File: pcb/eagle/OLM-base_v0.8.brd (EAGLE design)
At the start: 94.7 x 56.5 mm, 33 parts, among them IC1 ATMEGA, IC2 MCP1702-33, IC3 ENC28J60SP, J1 MAGJACK, J2 POWER_JACKPTH, X1 16 MHz, X3 25MHz

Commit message: changed logo
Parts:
- moved FTDI 12.8 mm to (11.6, 54.2), turned to 0 degrees
- moved R6 7.39 mm to (28.7, 19.5)
- moved R9 6.78 mm to (28.8, 30.3)
- moved C7 3.83 mm to (28.6, 42.1)
- moved C8 3.76 mm to (21.1, 42.1)
- moved CX2 3.50 mm to (29.0, 9.42)
- moved C5 3.48 mm to (21.3, 3.28), turned to 180 degrees
- moved R7 2.69 mm to (22.3, 34.2)
- moved R8 2.67 mm to (22.3, 38.1)
- moved CX1 1.98 mm to (21.7, 28.4)
- moved L1 1.86 mm to (34.0, 3.38)
- moved IC3 1.17 mm to (37.9, 27.2), turned to 270 degrees
- moved C2 0.98 mm to (66.4, 42.7)
- moved R4 0.74 mm to (20.4, 7.52)
- moved IC1 0.72 mm to (77.2, 28.3)
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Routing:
- net PB1/D9/PWM: track 167.5 -> 89.0 mm, vias 1 -> 2
- net N$52: track 36.6 -> 75.3 mm, vias 0 -> 1
- net N$37: track 11.1 -> 45.3 mm
- net TD-: track 19.6 -> 52.7 mm, vias 0 -> 2
- net N$39: track 21.3 -> 52.2 mm, vias 0 -> 2
- net N$50: track 31.2 -> 60.1 mm, vias 0 -> 2
- net D0/RX: track 96.4 -> 70.1 mm, vias 1 -> 4
- net SCK/D13: track 167.0 -> 186.7 mm, vias 1 -> 3
- net D1/TX: track 108.5 -> 90.2 mm, vias 2 -> 4
- net N$53: track 22.7 -> 38.8 mm, vias 0 -> 1
- net D4: track 37.5 -> 53.3 mm, vias 1 -> 2
- net N$20: track 62.6 -> 47.3 mm, vias 3 -> 1
- net N$51: track 52.4 -> 37.5 mm, vias 1 -> 0
- net VCC: track 218.9 -> 233.7 mm
- net LEDB: track 58.0 -> 43.7 mm
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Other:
- board text added: "(cable)"
- board text added: "3.3V"
- board text added: "5V"
- board text added: "A"
- board text added: "D"
- board text added: "D/PWM"
- board text added: "DTR"
- board text added: "GND"
- board text added: "MISO"
- board text added: "MISO/D12"
- board text added: "MOSI"
- board text added: "MOSI/D11"
- board text added: "PB0"
- board text added: "PB1"
- board text added: "RST"
- board text added: "RX"
- board text added: "SCK"
- board text added: "SCK/D13"
- board text added: "SCL/A5"
- board text added: "SDA/A4"
- board text added: "TX"
- board text added: "http://pvos.org"
- board text added: "lab"
- board text added: "monitor"
- board text added: "olm connector"
- board text added: "open"
- board text added: "v_0.8"
- board text removed: "PVOS.org"
- board text removed: "olm_v0.8"

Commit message: changed logo
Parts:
- moved C7 3.48 mm to (25.5, 43.6), turned to 270 degrees
- moved C8 2.98 mm to (18.5, 43.6), turned to 270 degrees
- moved R6 1.61 mm to (28.8, 21.1)
- moved IC2 1.20 mm to (4.57, 23.0), turned to 0 degrees
- moved CON1 1.19 mm to (64.0, 50.6)
- moved R9 1.10 mm to (28.9, 31.4)
- moved CON4 1.09 mm to (64.3, 5.13)
- moved X3 0.86 mm to (20.5, 16.8)
- moved CON3 0.74 mm to (89.6, 17.4)
- moved CON2 0.60 mm to (89.6, 39.0)
- moved C4 0.40 mm to (21.7, 22.7)
- moved CX2 0.39 mm to (28.9, 9.80)
- moved C3 0.38 mm to (14.1, 23.6)
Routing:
- net N$37: track 45.3 -> 71.0 mm, vias 0 -> 1
- net N$1: track 31.9 -> 54.5 mm, vias 2 -> 1
- net N$52: track 75.3 -> 55.6 mm
- net MISO/D12: track 180.5 -> 164.1 mm
- net SCL/A5: track 101.3 -> 116.9 mm
- net PB0/D8: track 92.6 -> 78.5 mm, vias 3 -> 2
- net TCT: track 66.2 -> 52.2 mm
- net SCK/D13: track 186.7 -> 173.4 mm, vias 3 -> 2
- net D5/PWM: track 33.3 -> 23.2 mm
- net GND: track 329.5 -> 319.9 mm
- net PB1/D9/PWM: track 89.0 -> 98.2 mm
- net D4: track 53.3 -> 44.3 mm, vias 2 -> 1
- net D1/TX: track 90.2 -> 82.0 mm, vias 4 -> 0
- net D10/PWM: track 19.6 -> 27.0 mm
- net D0/RX: track 70.1 -> 63.1 mm, vias 4 -> 3
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
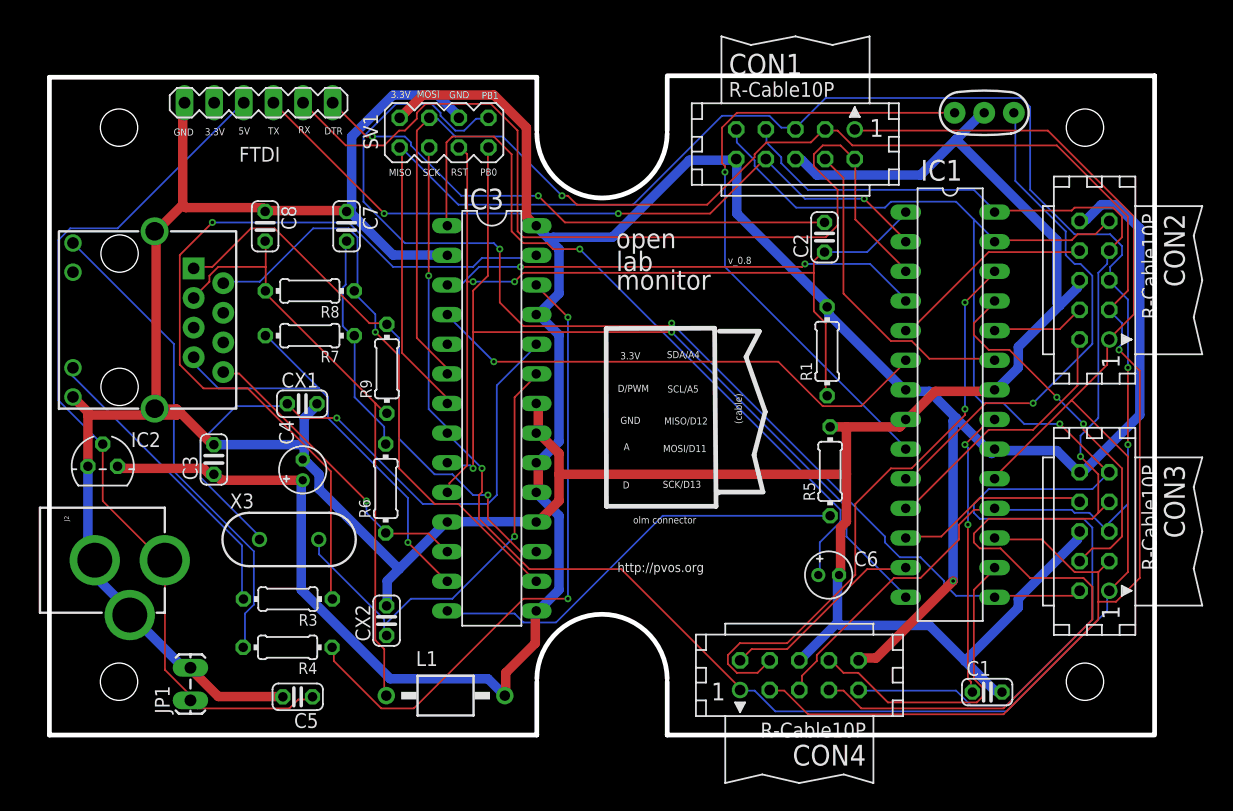
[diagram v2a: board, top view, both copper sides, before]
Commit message: fixed logo
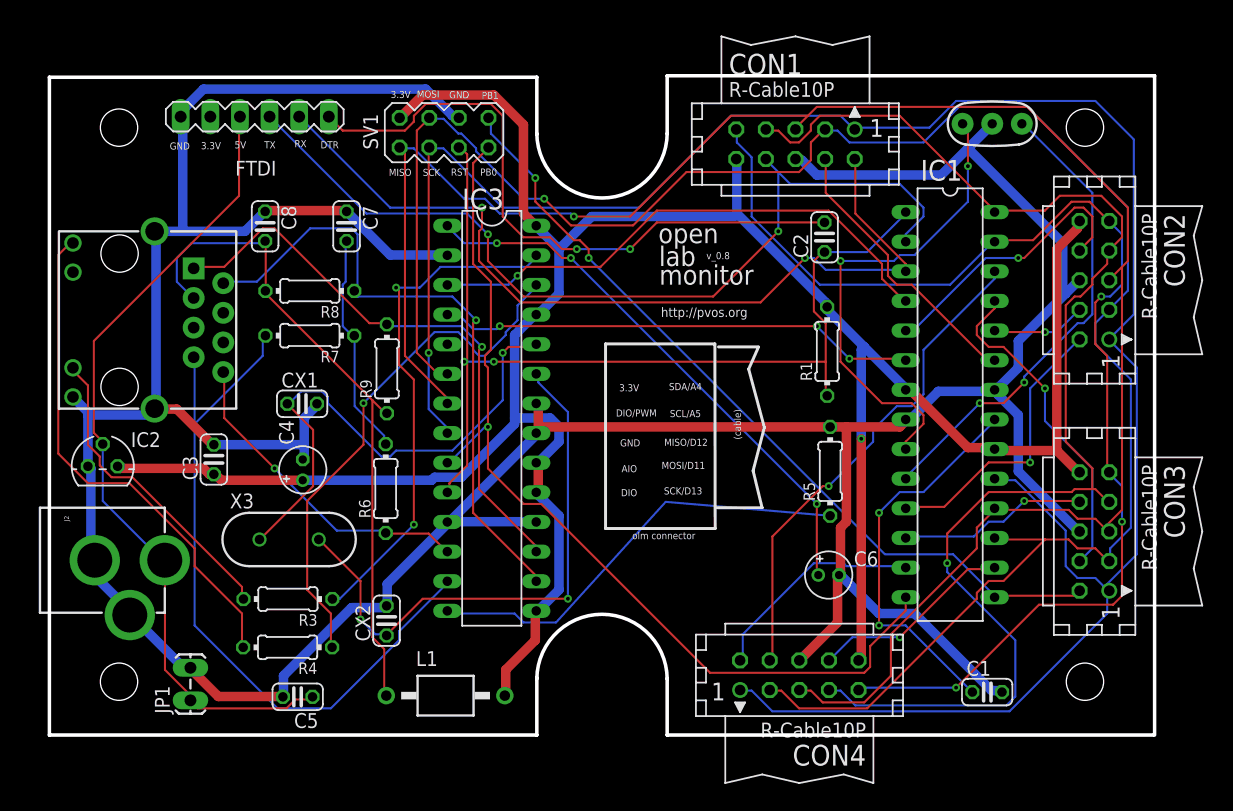
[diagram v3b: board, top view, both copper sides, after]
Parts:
- moved FTDI 1.24 mm to (11.3, 53.0)
- moved X1 1.16 mm to (80.8, 52.4)
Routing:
- net PB1/D9/PWM: track 98.2 -> 70.4 mm
- net N$37: track 71.0 -> 43.8 mm, vias 1 -> 2
- net RD+: track 39.8 -> 62.7 mm, vias 1 -> 0
- net SDA/A4: track 123.2 -> 105.8 mm, vias 1 -> 3
- net N$50: track 64.8 -> 47.8 mm, vias 1 -> 3
- net VCC: track 233.3 -> 216.7 mm
- net SCK/D13: track 173.4 -> 189.1 mm, vias 2 -> 1
- net D0/RX: track 63.1 -> 77.5 mm, vias 3 -> 2
- net N$1: track 54.5 -> 41.1 mm, vias 1 -> 2
- net N$52: track 55.6 -> 45.3 mm
- net D10/PWM: track 27.0 -> 17.6 mm, vias 0 -> 1
- net N$39: track 54.9 -> 45.6 mm, vias 2 -> 1
- net N$20: track 46.6 -> 55.4 mm
- net GND: track 319.9 -> 328.7 mm
- net N$53: track 39.7 -> 48.4 mm, vias 1 -> 2
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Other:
- outline, holes or cut-outs redrawn
- board text added: "AIO"
- board text added: "DIO"
- board text added: "DIO/PWM"
- board text removed: "A"
- board text removed: "D"
- board text removed: "D/PWM"
